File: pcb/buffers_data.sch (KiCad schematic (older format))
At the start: 10 parts

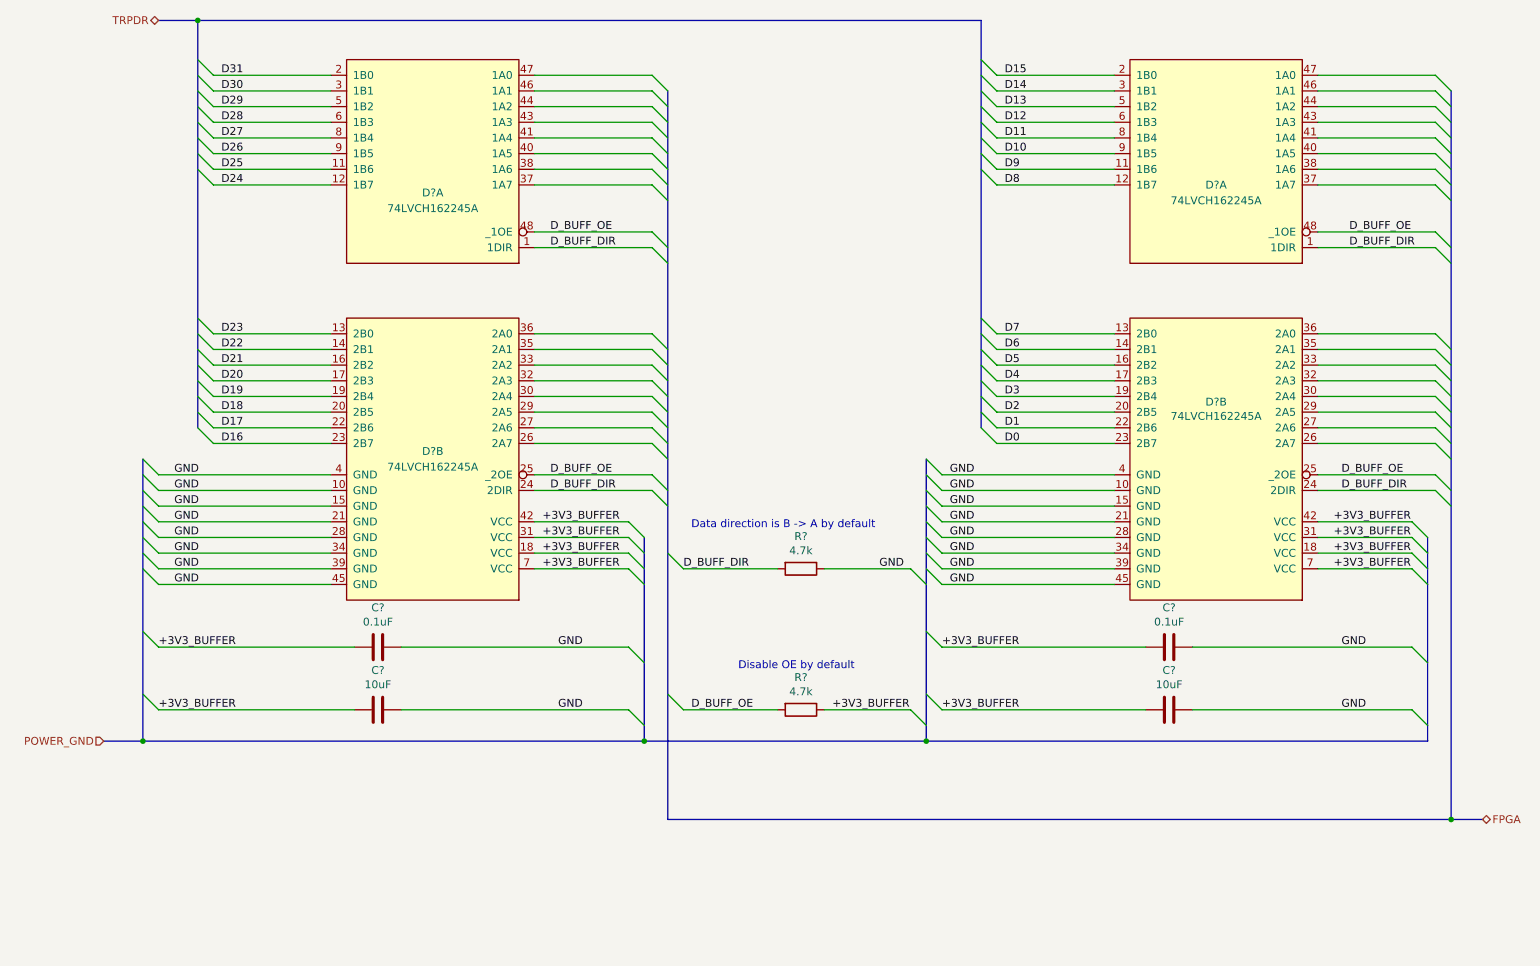
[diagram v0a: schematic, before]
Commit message: FPGA side labels added
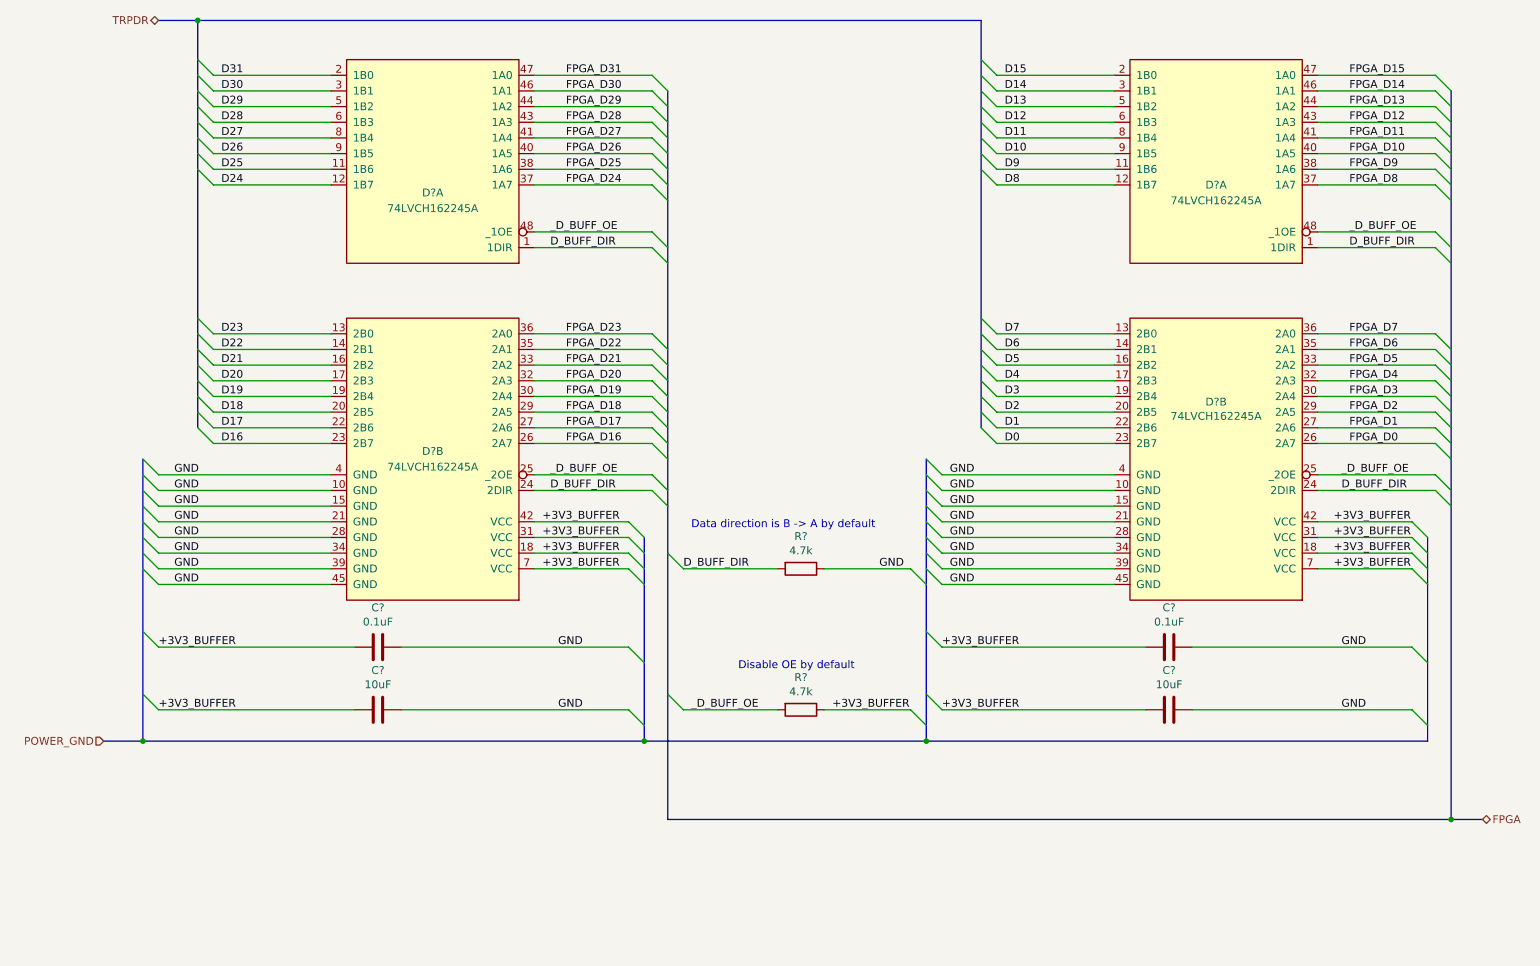
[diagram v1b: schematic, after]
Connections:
- net FPGA_D24: now reaches D?.37 (1A7)
- net FPGA_D25: now reaches D?.38 (1A6)
- net FPGA_D26: now reaches D?.40 (1A5)
- net FPGA_D27: now reaches D?.41 (1A4)
- net FPGA_D28: now reaches D?.43 (1A3)
- net FPGA_D29: now reaches D?.44 (1A2)
- net FPGA_D30: now reaches D?.46 (1A1)
- net FPGA_D31: now reaches D?.47 (1A0)
- net FPGA_D16: now reaches D?.26 (2A7)
- net FPGA_D17: now reaches D?.27 (2A6)
- net FPGA_D18: now reaches D?.29 (2A5)
- net FPGA_D19: now reaches D?.30 (2A4)
- net FPGA_D20: now reaches D?.32 (2A3)
- net FPGA_D21: now reaches D?.33 (2A2)
- net FPGA_D22: now reaches D?.35 (2A1)
- net FPGA_D23: now reaches D?.36 (2A0)
- net FPGA_D8: now reaches D?.37 (1A7)
- net FPGA_D9: now reaches D?.38 (1A6)
- net FPGA_D10: now reaches D?.40 (1A5)
- net FPGA_D11: now reaches D?.41 (1A4)
- net FPGA_D12: now reaches D?.43 (1A3)
- net FPGA_D13: now reaches D?.44 (1A2)
- net FPGA_D14: now reaches D?.46 (1A1)
- net FPGA_D15: now reaches D?.47 (1A0)
- net FPGA_D0: now reaches D?.26 (2A7)
- net FPGA_D1: now reaches D?.27 (2A6)
- net FPGA_D2: now reaches D?.29 (2A5)
- net FPGA_D3: now reaches D?.30 (2A4)
- net FPGA_D4: now reaches D?.32 (2A3)
- net FPGA_D5: now reaches D?.33 (2A2)
- net FPGA_D6: now reaches D?.35 (2A1)
- net FPGA_D7: now reaches D?.36 (2A0)
- net D_BUFF_OE renamed _D_BUFF_OE
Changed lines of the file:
@@
 GND
 Text Label 4000 4100 0    50   ~ 0
-D_BUFF_OE
+_D_BUFF_OE
 Text Label 4000 4200 0    50   ~ 0
 D_BUFF_DIR
@@
 D_BUFF_DIR
 Text Label 4900 5600 0    50   ~ 0
-D_BUFF_OE
+_D_BUFF_OE
 Text Label 5800 5600 0    50   ~ 0
 +3V3_BUFFER
@@
 Data direction is B -> A by default
 Text Label 4000 2550 0    50   ~ 0
-D_BUFF_OE
+_D_BUFF_OE
 Text Label 9100 2550 0    50   ~ 0
-D_BUFF_OE
+_D_BUFF_OE
 Text Label 4000 2650 0    50   ~ 0
 D_BUFF_DIR
@@
 D_BUFF_DIR
 Text Label 9050 4100 0    50   ~ 0
-D_BUFF_OE
+_D_BUFF_OE
+Wire Bus Line
+	1400 5800 4600 5800
+Text Label 4100 1550 0    50   ~ 0
+FPGA_D31
+Text Label 4100 1650 0    50   ~ 0
+FPGA_D30
+Text Label 4100 1750 0    50   ~ 0
+FPGA_D29
+Text Label 4100 1850 0    50   ~ 0
+FPGA_D28
+Text Label 4100 1950 0    50   ~ 0
+FPGA_D27
+Text Label 4100 2050 0    50   ~ 0
+FPGA_D26
+Text Label 4100 2150 0    50   ~ 0
+FPGA_D25
+Text Label 4100 2250 0    50   ~ 0
+FPGA_D24
+Text Label 4100 3200 0    50   ~ 0
+FPGA_D23
+Text Label 4100 3300 0    50   ~ 0
+FPGA_D22
+Text Label 4100 3400 0    50   ~ 0
+FPGA_D21
+Text Label 4100 3500 0    50   ~ 0
+FPGA_D20
+Text Label 4100 3600 0    50   ~ 0
+FPGA_D19
+Text Label 4100 3700 0    50   ~ 0
+FPGA_D18
+Text Label 4100 3800 0    50   ~ 0
+FPGA_D17
+Text Label 4100 3900 0    50   ~ 0
+FPGA_D16
+Text Label 9100 1550 0    50   ~ 0
+FPGA_D15
+Text Label 9100 1650 0    50   ~ 0
+FPGA_D14
+Text Label 9100 1750 0    50   ~ 0
+FPGA_D13
+Text Label 9100 1850 0    50   ~ 0
+FPGA_D12
+Text Label 9100 1950 0    50   ~ 0
+FPGA_D11
+Text Label 9100 2050 0    50   ~ 0
+FPGA_D10
+Text Label 9100 2150 0    50   ~ 0
+FPGA_D9
+Text Label 9100 2250 0    50   ~ 0
+FPGA_D8
+Text Label 9100 3200 0    50   ~ 0
+FPGA_D7
+Text Label 9100 3300 0    50   ~ 0
+FPGA_D6
+Text Label 9100 3400 0    50   ~ 0
+FPGA_D5
+Text Label 9100 3900 0    50   ~ 0
+FPGA_D0
+Text Label 9100 3800 0    50   ~ 0
+FPGA_D1
+Text Label 9100 3700 0    50   ~ 0
+FPGA_D2
+Text Label 9100 3600 0    50   ~ 0
+FPGA_D3
+Text Label 9100 3500 0    50   ~ 0
+FPGA_D4
 Wire Bus Line
 	4600 4500 4600 5800
@@
 Wire Bus Line
 	4750 1650 4750 6300
-Wire Bus Line
-	1400 5800 4600 5800
 $EndSCHEMATC

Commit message: Some work done on the whole project
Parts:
- removed C? (x2): 10uF, symbol Device:C
- removed C?: 0.1uF, symbol Device:C
- removed D? (x3): 74LVCH162245A, symbol WM1200:74LVCH162245A
- added C1: 0.1uF, symbol Device:C
- added C2, C4: 10uF, symbol Device:C
- added U1: 74LVCH162245A, symbol WM1200:74LVCH162245A
- added unit 1 of U2
- gave numbers to parts that had none: 4
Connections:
- net +3V3_BUFFER: now also C1.1, C2.1, C4.1, U1.18 (VCC), U1.31 (VCC), U1.42 (VCC), U1.7 (VCC)
- net D10: now also U2.9 (1B5)
- net D11: now also U2.8 (1B4)
- net D12: now also U2.6 (1B3)
- net D13: now also U2.5 (1B2)
- net D14: now also U2.3 (1B1)
- net D15: now also U2.2 (1B0)
- net D16: now also U1.23 (2B7)
- net D17: now also U1.22 (2B6)
- net D18: now also U1.20 (2B5)
- net D19: now also U1.19 (2B4)
- net D20: now also U1.17 (2B3)
- net D21: now also U1.16 (2B2)
- net D22: now also U1.14 (2B1)
- net D23: now also U1.13 (2B0)
- net D24: now also U1.12 (1B7)
- net D25: now also U1.11 (1B6)
- net D26: now also U1.9 (1B5)
- net D27: now also U1.8 (1B4)
- net D28: now also U1.6 (1B3)
- net D29: now also U1.5 (1B2)
- net D30: now also U1.3 (1B1)
- net D31: now also U1.2 (1B0)
- net D8: now also U2.12 (1B7)
- net D9: now also U2.11 (1B6)
- net D_BUFF_DIR: now also U1.1 (1DIR), U1.24 (2DIR), U2.1 (1DIR)
- net FPGA_D10: now also U2.40 (1A5)
- net FPGA_D11: now also U2.41 (1A4)
- net FPGA_D12: now also U2.43 (1A3)
- net FPGA_D13: now also U2.44 (1A2)
- net FPGA_D14: now also U2.46 (1A1)
- net FPGA_D15: now also U2.47 (1A0)
- net FPGA_D16: now also U1.26 (2A7)
- net FPGA_D17: now also U1.27 (2A6)
- net FPGA_D18: now also U1.29 (2A5)
- net FPGA_D19: now also U1.30 (2A4)
- net FPGA_D20: now also U1.32 (2A3)
- net FPGA_D21: now also U1.33 (2A2)
- net FPGA_D22: now also U1.35 (2A1)
- net FPGA_D23: now also U1.36 (2A0)
- net FPGA_D24: now also U1.37 (1A7)
- net FPGA_D25: now also U1.38 (1A6)
- net FPGA_D26: now also U1.40 (1A5)
- net FPGA_D27: now also U1.41 (1A4)
- net FPGA_D28: now also U1.43 (1A3)
- net FPGA_D29: now also U1.44 (1A2)
- net FPGA_D30: now also U1.46 (1A1)
- net FPGA_D31: now also U1.47 (1A0)
- net FPGA_D8: now also U2.37 (1A7)
- net FPGA_D9: now also U2.38 (1A6)
- net GND: now also C1.2, C2.2, C4.2, U1.10 (GND), U1.15 (GND), U1.21 (GND), U1.28 (GND), U1.34 (GND), U1.39 (GND), U1.4 (GND), U1.45 (GND)
- net _D_BUFF_OE: now also U1.25 (_2OE), U1.48 (_1OE), U2.48 (_1OE)
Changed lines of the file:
@@
 $Descr A4 11693 8268
 encoding utf-8
-Sheet 8 11
+Sheet 7 11
 Title "WishMaster 1200"
 Date ""
@@
 $EndDescr
 $Comp
-L WM1200:74LVCH162245A D?
-U 1 1 5E552A9B
+L WM1200:74LVCH162245A U1
+U 1 1 5E91F41D
 P 3250 2750
-F 0 "D?" H 3250 3200 50  0000 C CNN
+F 0 "U1" H 3250 3200 50  0000 C CNN
 F 1 "74LVCH162245A" H 3250 3100 50  0000 C CNN
 F 2 "" H 3250 2750 50  0001 C CNN
@@
 $EndComp
 $Comp
-L WM1200:74LVCH162245A D?
-U 2 1 5E556C63
+L WM1200:74LVCH162245A U1
+U 2 1 5E91F41F
 P 3250 4900
-F 0 "D?" H 3250 5850 50  0000 C CNN
+F 0 "U1" H 3250 5850 50  0000 C CNN
 F 1 "74LVCH162245A" H 3250 5750 50  0000 C CNN
 F 2 "" H 3250 4900 50  0001 C CNN
@@
 $EndComp
 $Comp
-L WM1200:74LVCH162245A D?
-U 1 1 5E5582DD
+L WM1200:74LVCH162245A U2
+U 1 1 5E91F420
 P 8250 2750
-F 0 "D?" H 8250 3250 50  0000 C CNN
+F 0 "U2" H 8250 3250 50  0000 C CNN
 F 1 "74LVCH162245A" H 8250 3150 50  0000 C CNN
 F 2 "" H 8250 2750 50  0001 C CNN
@@
 $EndComp
 $Comp
-L WM1200:74LVCH162245A D?
+L WM1200:74LVCH162245A U2
 U 2 1 5E55BDDA
 P 8250 4900
-F 0 "D?" H 8250 6165 50  0000 C CNN
+F 0 "U2" H 8250 6165 50  0000 C CNN
 F 1 "74LVCH162245A" H 8250 6074 50  0000 C CNN
 F 2 "" H 8250 4900 50  0001 C CNN
@@
 	9500 4700 8900 4700
 $Comp
-L Device:C C?
-U 1 1 5E78F0E1
+L Device:C C2
+U 1 1 5E91F423
 P 2900 5600
-F 0 "C?" V 3152 5600 50  0000 C CNN
+F 0 "C2" V 3152 5600 50  0000 C CNN
 F 1 "10uF" V 3061 5600 50  0000 C CNN
 F 2 "" H 2938 5450 50  0001 C CNN
@@
 $EndComp
 $Comp
-L Device:C C?
-U 1 1 5E78FE60
+L Device:C C1
+U 1 1 5E91F425
 P 2900 5200
-F 0 "C?" V 3152 5200 50  0000 C CNN
+F 0 "C1" V 3152 5200 50  0000 C CNN
 F 1 "0.1uF" V 3061 5200 50  0000 C CNN
 F 2 "" H 2938 5050 50  0001 C CNN
@@
 $EndComp
 $Comp
-L Device:C C?
-U 1 1 5E79CB26
+L Device:C C4
+U 1 1 5E91F426
 P 7950 5600
-F 0 "C?" V 8202 5600 50  0000 C CNN
+F 0 "C4" V 8202 5600 50  0000 C CNN
 F 1 "10uF" V 8111 5600 50  0000 C CNN
 F 2 "" H 7988 5450 50  0001 C CNN
@@
 $EndComp
 $Comp
-L Device:C C?
+L Device:C C3
 U 1 1 5E79CB2C
 P 7950 5200
-F 0 "C?" V 8202 5200 50  0000 C CNN
+F 0 "C3" V 8202 5200 50  0000 C CNN
 F 1 "0.1uF" V 8111 5200 50  0000 C CNN
 F 2 "" H 7988 5050 50  0001 C CNN
@@
 D_BUFF_DIR
 $Comp
-L Device:R R?
+L Device:R R13
 U 1 1 5E7D2869
 P 5600 4700
-F 0 "R?" V 5393 4700 50  0000 C CNN
+F 0 "R13" V 5393 4700 50  0000 C CNN
 F 1 "4.7k" V 5484 4700 50  0000 C CNN
 F 2 "" V 5530 4700 50  0001 C CNN
@@
 $EndComp
 $Comp
-L Device:R R?
+L Device:R R14
 U 1 1 5E7D396E
 P 5600 5600
-F 0 "R?" V 5393 5600 50  0000 C CNN
+F 0 "R14" V 5393 5600 50  0000 C CNN
 F 1 "4.7k" V 5484 5600 50  0000 C CNN
 F 2 "" V 5530 5600 50  0001 C CNN

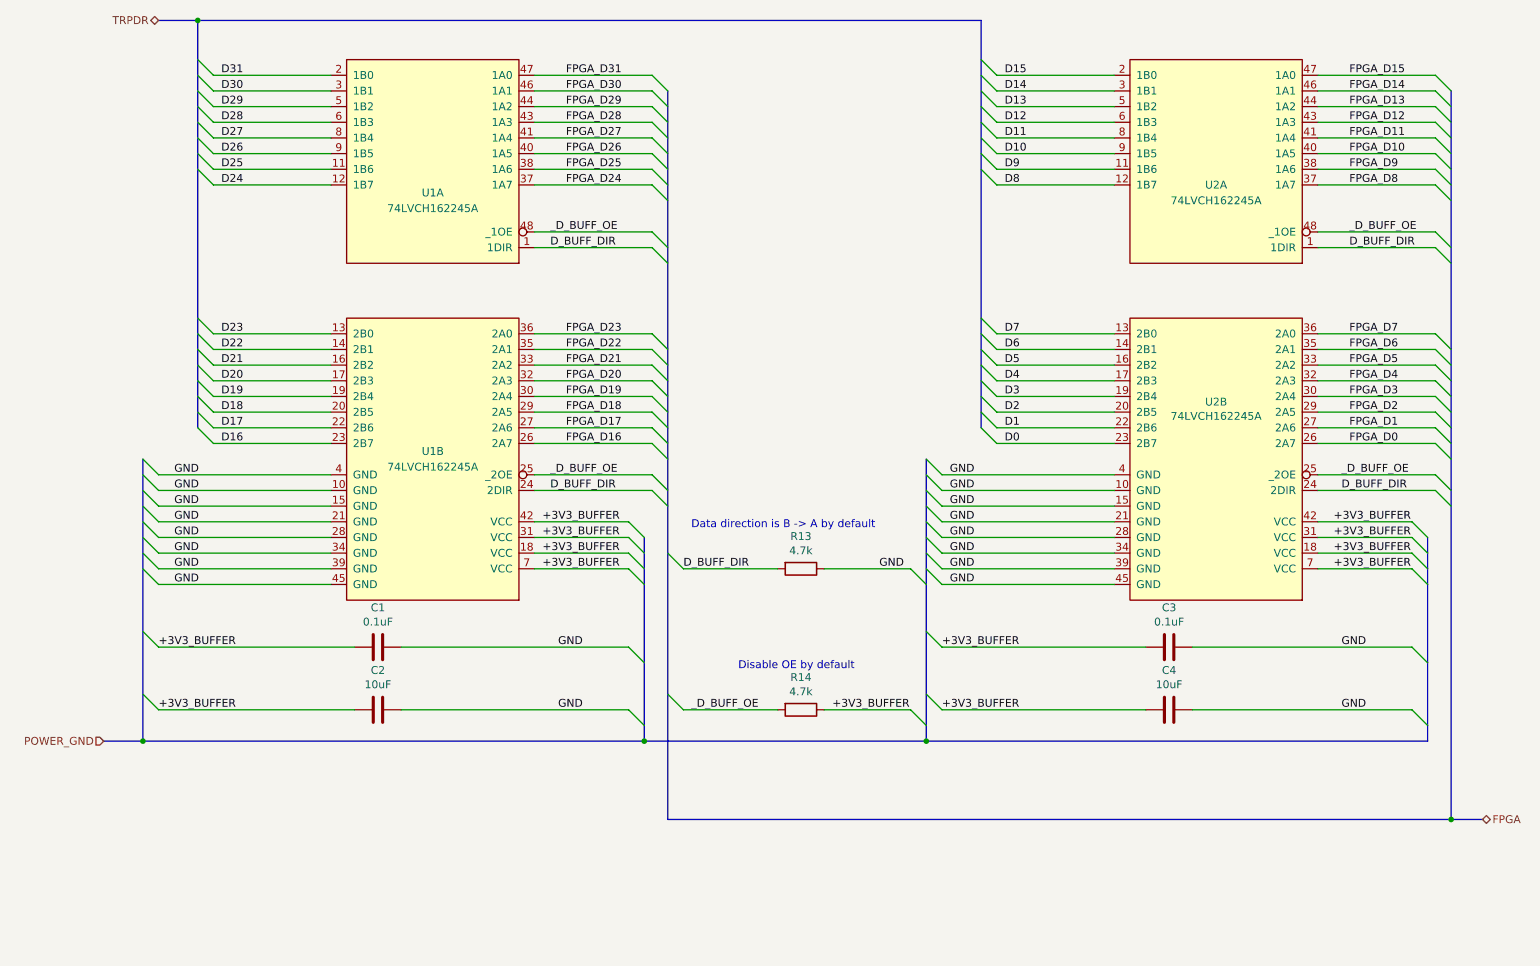
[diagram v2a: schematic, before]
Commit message: ok, we are using global labels now
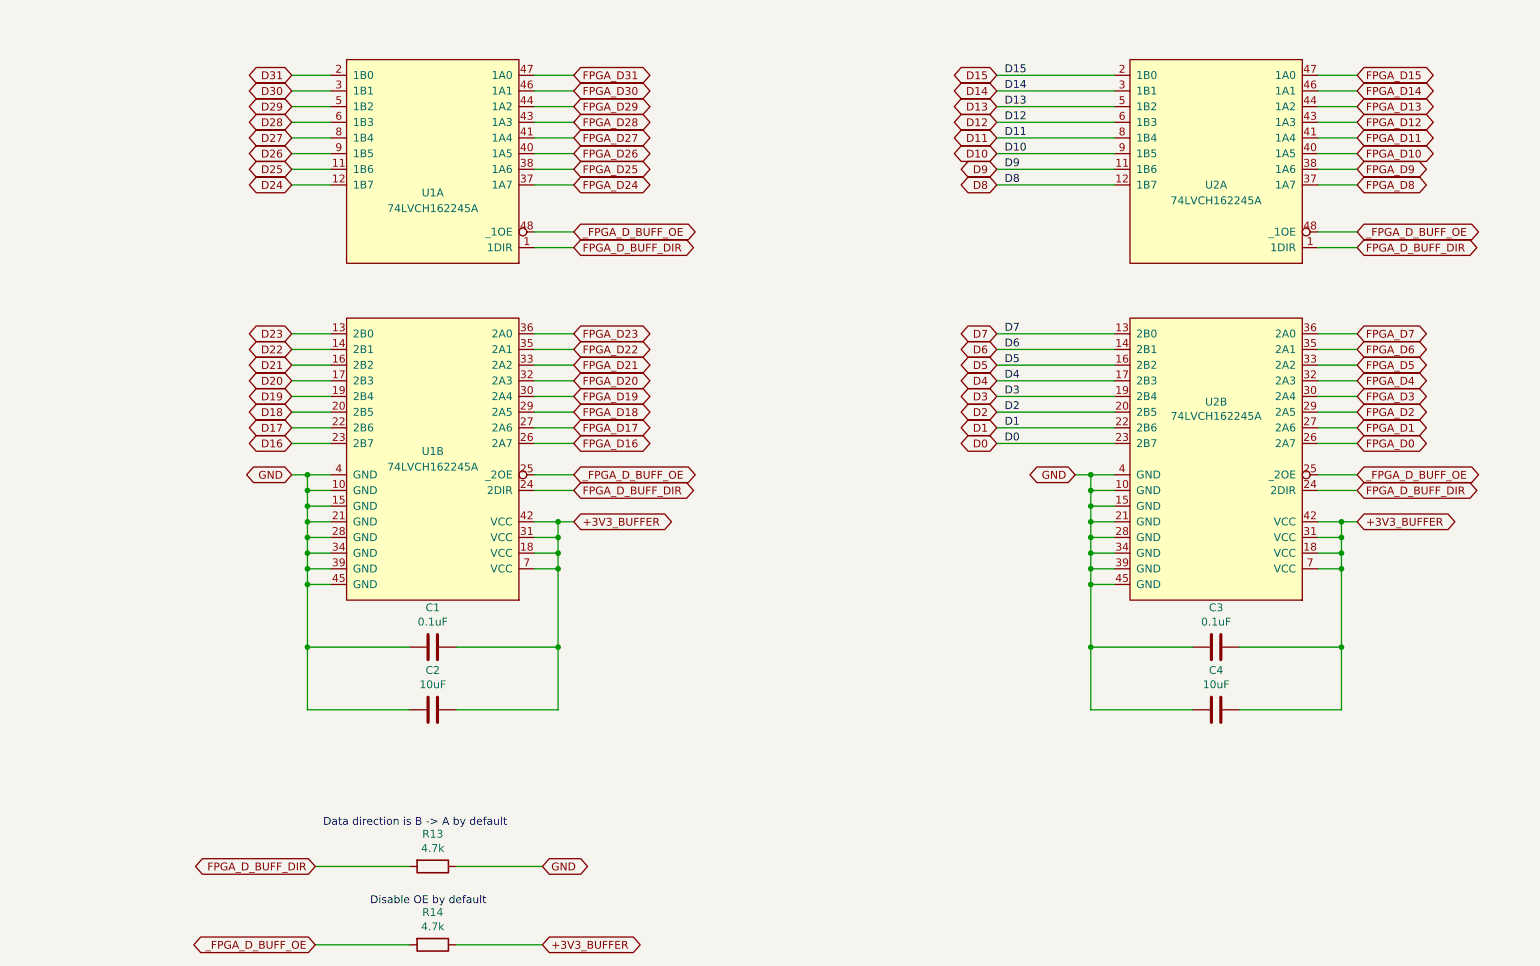
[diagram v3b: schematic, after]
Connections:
- net +3V3_BUFFER: now also C1.2, C2.2, C3.2, C4.2; no longer C1.1, C2.1, C3.1, C4.1
- net GND: now also C1.1, C2.1, C3.1, C4.1; no longer C1.2, C2.2, C3.2, C4.2
- net D_BUFF_DIR renamed FPGA_D_BUFF_DIR
- net _D_BUFF_OE renamed _FPGA_D_BUFF_OE
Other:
- moved on the sheet: C1, C2, C3, C4, R13, R14

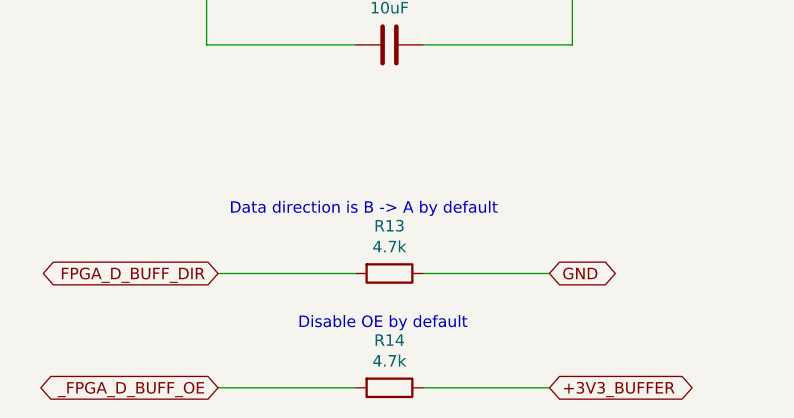
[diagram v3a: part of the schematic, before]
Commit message: fpga-side gpio connector added
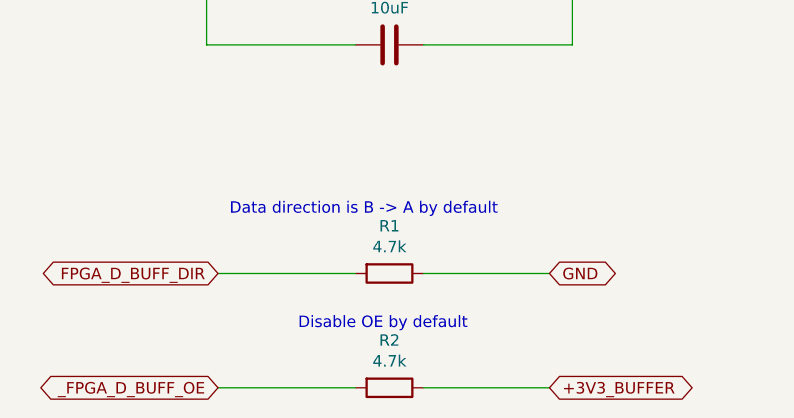
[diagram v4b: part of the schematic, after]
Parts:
- renumbered R13 to R1, R14 to R2
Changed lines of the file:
@@
 D0
 $Comp
-L Device:R R13
+L Device:R R1
 U 1 1 5E7D2869
 P 3250 6600
-F 0 "R13" V 3043 6600 50  0000 C CNN
+F 0 "R1" V 3043 6600 50  0000 C CNN
 F 1 "4.7k" V 3134 6600 50  0000 C CNN
 F 2 "" V 3180 6600 50  0001 C CNN
@@
 $EndComp
 $Comp
-L Device:R R14
+L Device:R R2
 U 1 1 5E7D396E
 P 3250 7100
-F 0 "R14" V 3043 7100 50  0000 C CNN
+F 0 "R2" V 3043 7100 50  0000 C CNN
 F 1 "4.7k" V 3134 7100 50  0000 C CNN
 F 2 "" V 3180 7100 50  0001 C CNN
